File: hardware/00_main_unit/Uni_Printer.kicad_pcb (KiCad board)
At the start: 4 copper layers, 81 x 127.5 mm, 179 parts, among them IC1 MAX17503ATP+, IC10 ITS4141NHUMA1, IC11 ITS4141NHUMA1, IC2 AM26C31CD, IC3 74HC14D, IC4 TLV1117-33, IC5 LAN8742A, IC6 ITS4141NHUMA1, IC7 ITS4141NHUMA1, IC8 ITS4141NHUMA1, IC9 ITS4141NHUMA1, J1 Conn_01x10, J10 USB B connector, J11 LMJ1998824110DL1T39J, J12 RJ45, J13 Conn_01x04_Male, J14 Conn_02x13_Odd_Even, J2 Conn_01x10, J3 Conn_01x10, J4 Conn_01x10, J5 FIDUCIAL, J6 FIDUCIAL, J7 Conn_01x10, J8 Conn_01x10, J9 RJ45, SW2 SW_Push, SW3 SW_Push, U1 STM32H743VIT6, U3 TLE9251VSJ, U5 ST1480ACDR, U6 ST1480ACDR, U7 ST1480ACDR, U8 ST1480ACDR, U9 ST1480ACDR, Y1 ABM7-25.000MHZ-D2Y-T, Y2 ABM7-25.000MHZ-D2Y-T

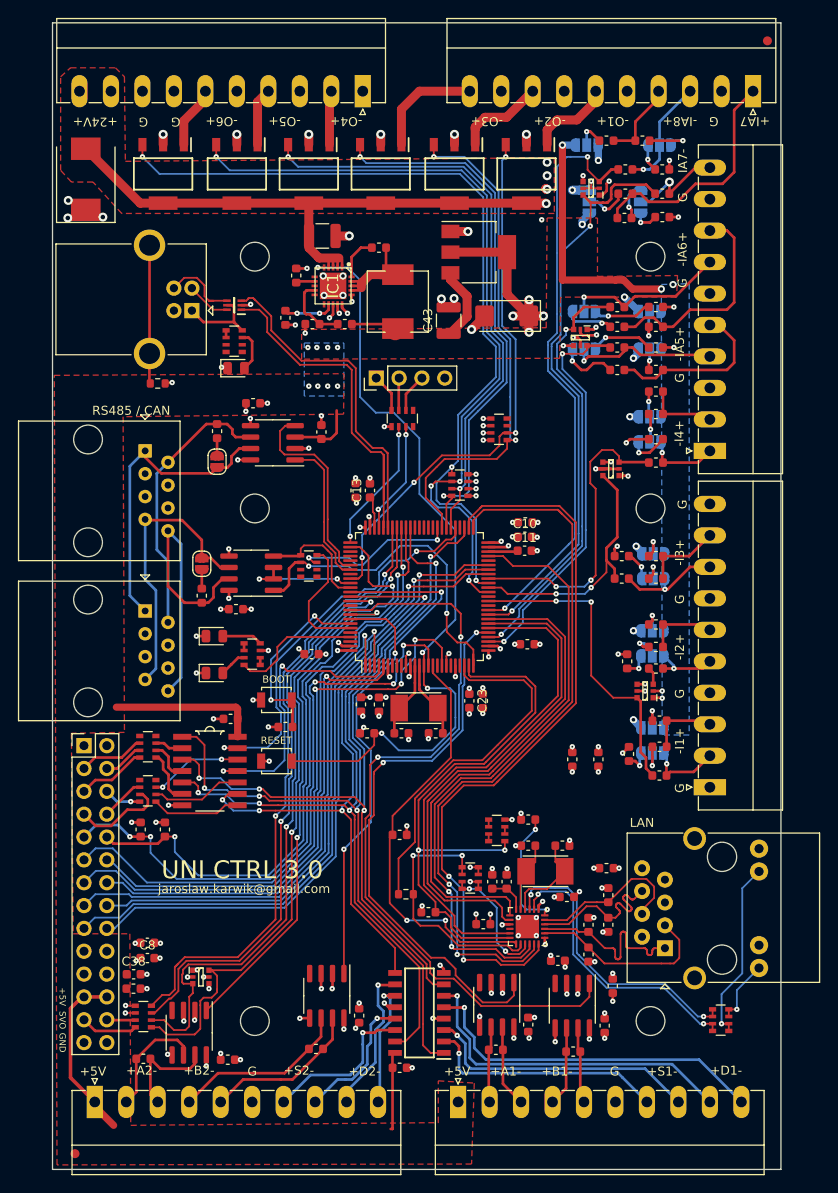
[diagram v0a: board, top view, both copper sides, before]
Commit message: Debug uart added
Signed-off-by: Jarosław Karwik <jaroslaw.karwik@gmail.com>
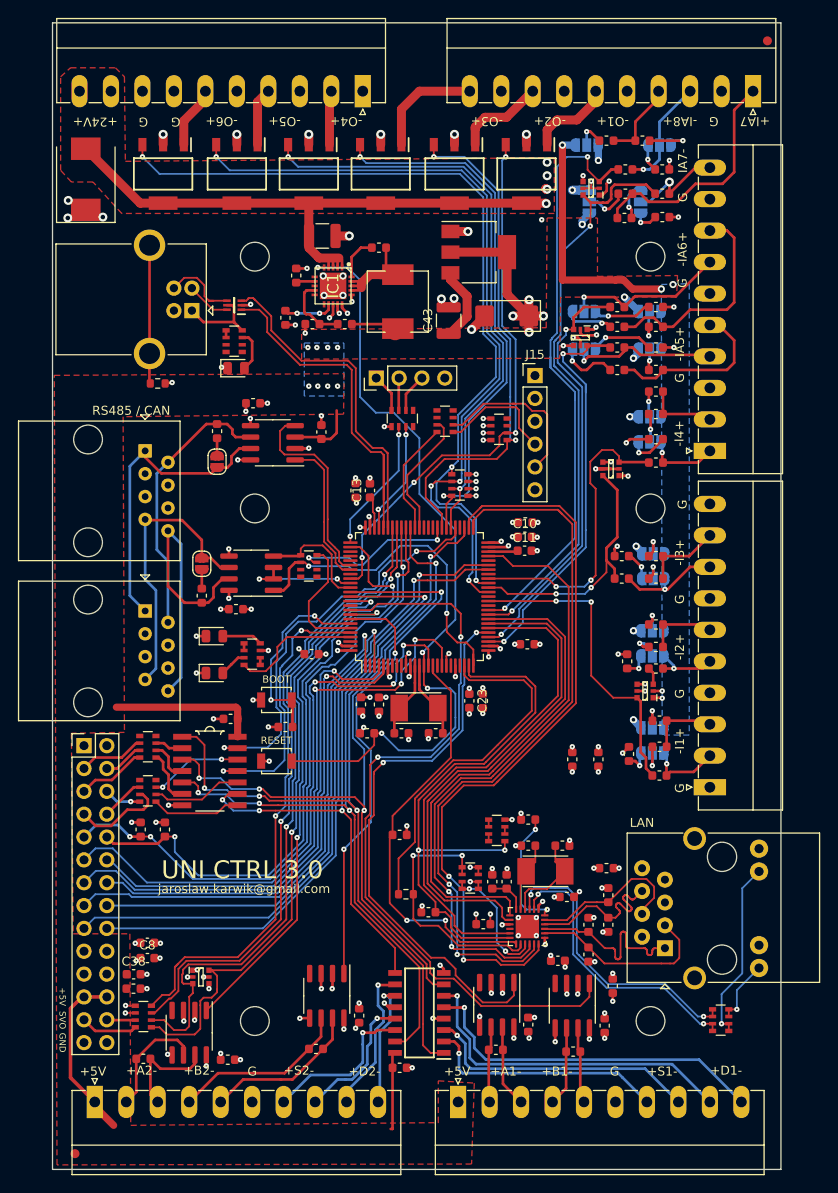
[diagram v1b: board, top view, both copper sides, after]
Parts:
- added J15: Conn_01x06_Male, Connector_PinHeader_2.54mm:PinHeader_1x06_P2.54mm_Vertical, F.Cu at (129.2, 55.2)
- added RN11: 100R, moje:R_Array_Convex_4x0603, F.Cu at (119.2, 60.3)
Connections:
- net /Digital Inputs/AIN_IN5 renamed /Connectors/AIN_IN5
- net /Digital Inputs/AIN_IN6 renamed /Connectors/AIN_IN6
- net /Digital Inputs/AIN_IN7 renamed /Connectors/AIN_IN7
- net /Digital Inputs/AIN_IN8 renamed /Connectors/AIN_IN8
- net /Digital Inputs/AIN_IN_SUP5 renamed /Connectors/AIN_IN_SUP5
- net /Digital Inputs/AIN_IN_SUP6 renamed /Connectors/AIN_IN_SUP6
- net /Digital Inputs/AIN_IN_SUP7 renamed /Connectors/AIN_IN_SUP7
- net /Digital Inputs/AIN_IN_SUP8 renamed /Connectors/AIN_IN_SUP8
- net /Digital Inputs/IN1 renamed /Connectors/IN1
- net /Digital Inputs/IN2 renamed /Connectors/IN2
- net /Digital Inputs/IN3 renamed /Connectors/IN3
- net /Digital Inputs/IN4 renamed /Connectors/IN4
- net /Digital Inputs/IN_SUP1 renamed /Connectors/IN_SUP1
- net /Digital Inputs/IN_SUP2 renamed /Connectors/IN_SUP2
- net /Digital Inputs/IN_SUP3 renamed /Connectors/IN_SUP3
- net /Digital Inputs/IN_SUP4 renamed /Connectors/IN_SUP4
- net /Encoder/ENC1_IN.A1 renamed /Connectors/ENC1_IN.A1
- net /Encoder/ENC1_IN.A2 renamed /Connectors/ENC1_IN.A2
- net /Encoder/ENC1_IN.B1 renamed /Connectors/ENC1_IN.B1
- net /Encoder/ENC1_IN.B2 renamed /Connectors/ENC1_IN.B2
- net /Encoder/ENC2_IN.A1 renamed /Connectors/ENC2_IN.A1
- net /Encoder/ENC2_IN.A2 renamed /Connectors/ENC2_IN.A2
- net /Encoder/ENC2_IN.B1 renamed /Connectors/ENC2_IN.B1
- net /Encoder/ENC2_IN.B2 renamed /Connectors/ENC2_IN.B2
- net /Outputs/OUT1 renamed /Connectors/OUT_HSW1
- net /Outputs/OUT2 renamed /Connectors/OUT_HSW2
- net /Outputs/OUT3 renamed /Connectors/OUT_HSW3
- net /Outputs/OUT4 renamed /Connectors/OUT_HSW4
- net /Outputs/OUT5 renamed /Connectors/OUT_HSW5
- net /Outputs/OUT6 renamed /Connectors/OUT_HSW6
- net /midboard/OUT_E1 renamed /Analod / Digital IO/OUT_E1
- net /midboard/OUT_E2 renamed /Analod / Digital IO/OUT_E2
- net /midboard/OUT_E3 renamed /Analod / Digital IO/OUT_E3
- net /midboard/OUT_E4 renamed /Analod / Digital IO/OUT_E4
- net /midboard/OUT_E5 renamed /Analod / Digital IO/OUT_E5
- net /midboard/OUT_E6 renamed /Analod / Digital IO/OUT_E6
- IC1 pad 10: (no net) -> unconnected-(IC1-Pad10)
- IC1 pad 11: (no net) -> unconnected-(IC1-Pad11)
- IC1 pad 6: (no net) -> unconnected-(IC1-Pad6)
- IC1 pad 8: (no net) -> unconnected-(IC1-Pad8)
- IC5 pad 10: (no net) -> unconnected-(IC5-Pad10)
- RN12 pad 3: (no net) -> unconnected-(RN12-Pad3)
- RN12 pad 4: (no net) -> unconnected-(RN12-Pad4)
- RN4 pad 1: (no net) -> unconnected-(RN4-Pad1)
- RN4 pad 2: (no net) -> unconnected-(RN4-Pad2)
- RN4 pad 7: (no net) -> unconnected-(RN4-Pad7)
- RN4 pad 8: (no net) -> unconnected-(RN4-Pad8)
- RN5 pad 4: (no net) -> unconnected-(RN5-Pad4)
- RN5 pad 5: (no net) -> unconnected-(RN5-Pad5)
- RN6 pad 4: (no net) -> unconnected-(RN6-Pad4)
- RN6 pad 5: (no net) -> unconnected-(RN6-Pad5)
- RN7 pad 4: (no net) -> unconnected-(RN7-Pad4)
- RN7 pad 5: (no net) -> unconnected-(RN7-Pad5)
- RN8 pad 1: (no net) -> unconnected-(RN8-Pad1)
- RN8 pad 2: (no net) -> unconnected-(RN8-Pad2)
- RN8 pad 7: (no net) -> unconnected-(RN8-Pad7)
- RN8 pad 8: (no net) -> unconnected-(RN8-Pad8)
- U1 pad 17: (no net) -> unconnected-(U1-Pad17)
- U1 pad 2: (no net) -> unconnected-(U1-Pad2)
- U1 pad 20: (no net) -> unconnected-(U1-Pad20)
- U1 pad 22: (no net) -> unconnected-(U1-Pad22)
- U1 pad 36: (no net) -> unconnected-(U1-Pad36)
- U1 pad 38: (no net) -> /IN_CPU2
- U1 pad 4: /OUT_STEP3 -> /SPI.MISO
- U1 pad 43: /SPI.MISO -> unconnected-(U1-Pad43)
- U1 pad 46: (no net) -> unconnected-(U1-Pad46)
- U1 pad 54: (no net) -> unconnected-(U1-Pad54)
- U1 pad 60: (no net) -> unconnected-(U1-Pad60)
- U1 pad 61: (no net) -> unconnected-(U1-Pad61)
- U1 pad 62: (no net) -> unconnected-(U1-Pad62)
- U1 pad 63: (no net) -> /Processor/UART6_TX__PC6
- U1 pad 64: (no net) -> /Processor/UART6_RX__PC7
- U1 pad 7: (no net) -> unconnected-(U1-Pad7)
- U1 pad 78: (no net) -> unconnected-(U1-Pad78)
- U1 pad 79: (no net) -> unconnected-(U1-Pad79)
- U1 pad 8: (no net) -> unconnected-(U1-Pad8)
- U1 pad 80: (no net) -> unconnected-(U1-Pad80)
- U1 pad 83: (no net) -> unconnected-(U1-Pad83)
- U1 pad 9: (no net) -> unconnected-(U1-Pad9)
- U1 pad 90: (no net) -> unconnected-(U1-Pad90)
- U1 pad 96: (no net) -> /OUT_STEP3
- U1 pad 98: (no net) -> unconnected-(U1-Pad98)
- U5 pad 4: (no net) -> unconnected-(U5-Pad4)
- U6 pad 4: (no net) -> unconnected-(U6-Pad4)
- U7 pad 4: (no net) -> unconnected-(U7-Pad4)
- U8 pad 4: (no net) -> unconnected-(U8-Pad4)
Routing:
- net Net-(J15-Pad5): track 0.00 -> 18.7 mm
- net /SPI.MISO: track 73.7 -> 56.8 mm
- net /Processor/UART6_TX__PC6: track 0.00 -> 14.2 mm
- net Net-(J15-Pad4): track 0.00 -> 13.3 mm
- net /Processor/UART6_RX__PC7: track 0.00 -> 12.7 mm
- net /AIN_IN_ADC8: track 65.8 -> 67.6 mm
- net /OUT_STEP3: track 31.9 -> 30.1 mm
- net /OUT_DIR3: track 44.1 -> 45.3 mm
- net /I2C.SCL: track 72.1 -> 71.1 mm
- net /Processor/BOOT0: track 21.0 -> 22.1 mm
- net /OUT_DIR2: track 73.1 -> 72.1 mm
- net /AIN_IN_ADC5: track 44.6 -> 45.4 mm
- net /OUT_STEP2: track 89.6 -> 88.9 mm
